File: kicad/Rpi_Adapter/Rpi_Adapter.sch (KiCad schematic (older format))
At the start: 4 parts, among them P1 CONN_02X20, P2 CONN_02X03

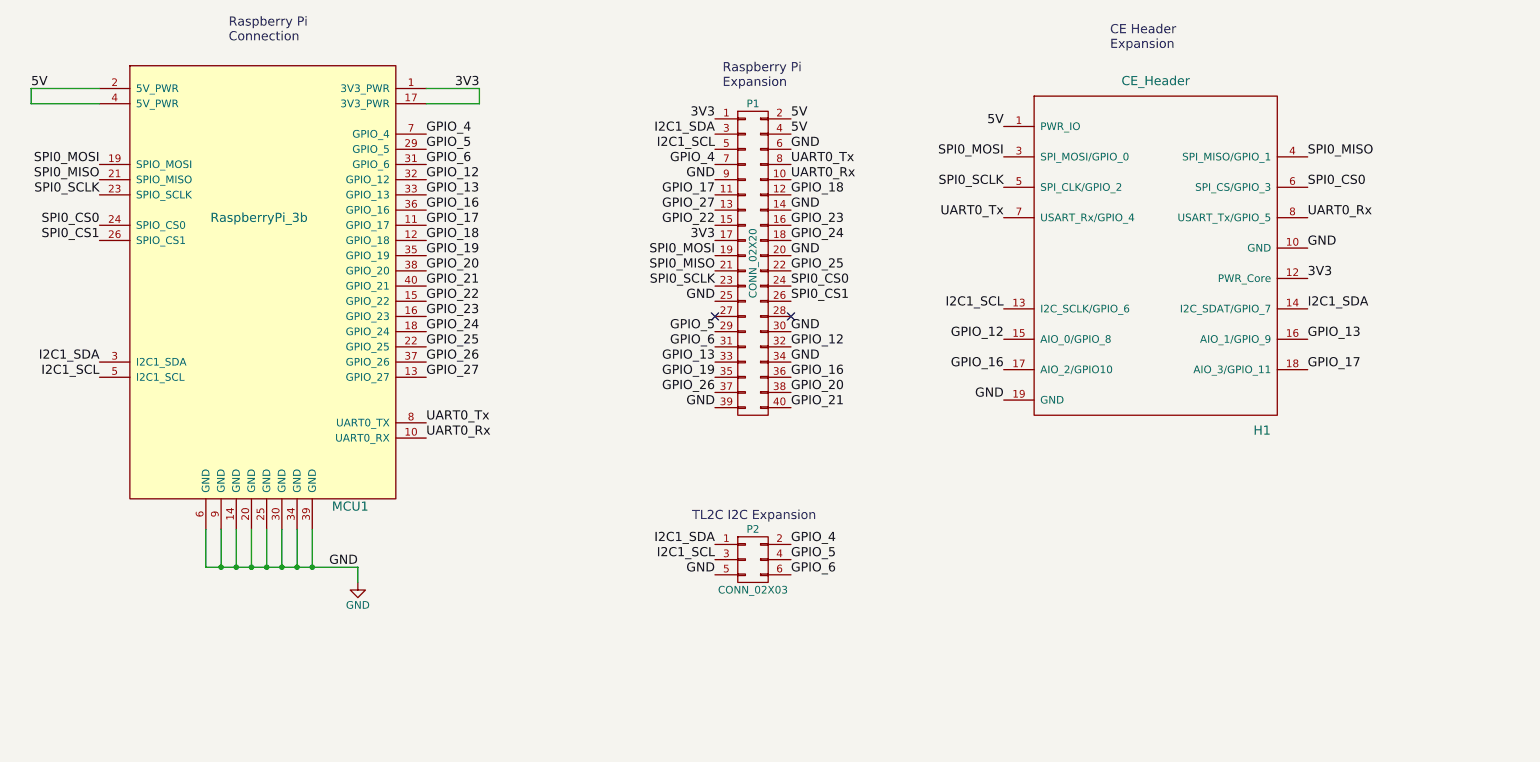
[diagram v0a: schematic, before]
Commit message: Layout done and 2L_1 is sent to OSH Park
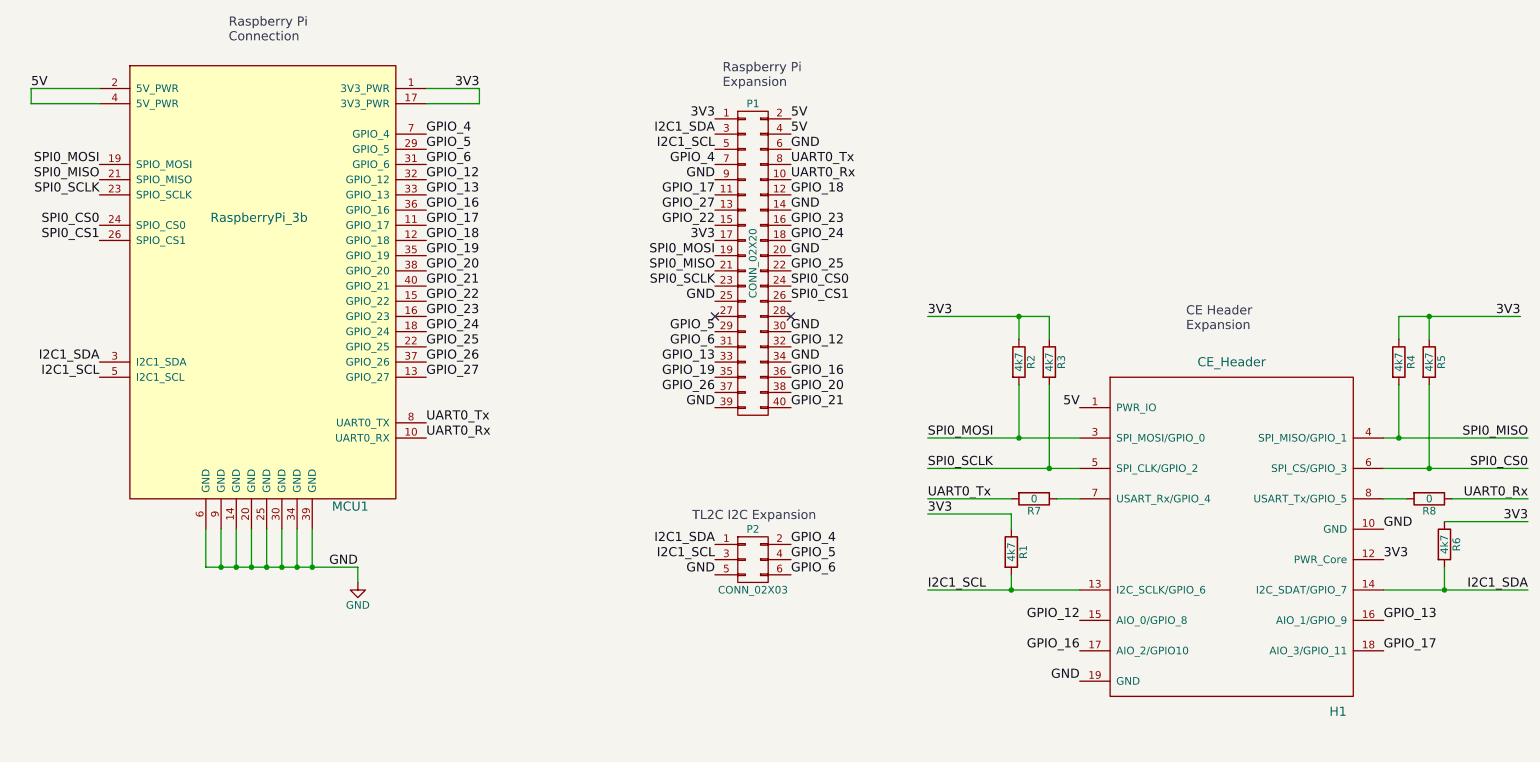
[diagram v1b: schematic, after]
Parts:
- added R1, R2, R3, R4, R5, R6: 4k7, Resistors_SMD:R_0805, symbol R
- added R7, R8: 0, Resistors_SMD:R_0805, symbol R
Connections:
- net 3V3: now also R1.1, R2.1, R3.1, R4.1, R5.1, R6.1
- net I2C1_SCL: now also R1.2
- net I2C1_SDA: now also R6.2
- net SPI0_CS0: now also R5.2
- net SPI0_MISO: now also R4.2
- net SPI0_MOSI: now also R2.2
- net SPI0_SCLK: now also R3.2
- net UART0_Rx: now also R8.1; no longer H1.8 (USART_Tx/GPIO_5)
- net UART0_Tx: now also R7.2; no longer H1.7 (USART_Rx/GPIO_4)
- new net: H1.7 (USART_Rx/GPIO_4), R7.1
- new net: H1.8 (USART_Tx/GPIO_5), R8.2
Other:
- moved on the sheet: H1
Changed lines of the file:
@@
 L CE_Header H1
 U 1 1 594798FD
-P 8500 2550
-F 0 "H1" H 9200 1350 60  0000 C CNN
-F 1 "CE_Header" H 8500 3650 60  0000 C CNN
-F 2 "CE_Header:CE_Header" H 8100 2950 60  0001 C CNN
-F 3 "" H 8100 2950 60  0000 C CNN
-	1    8500 2550
+P 9000 4400
+F 0 "H1" H 9700 3200 60  0000 C CNN
+F 1 "CE_Header" H 9000 5500 60  0000 C CNN
+F 2 "CE_Header:CE_Header" H 8600 4800 60  0001 C CNN
+F 3 "" H 8600 4800 60  0000 C CNN
+	1    9000 4400
 	1    0    0    -1
 $EndComp
@@
 Text Label 1550 3400 2    60   ~ 0
 I2C1_SCL
-Wire Wire Line
-	2250 4400 2250 4650
-Wire Wire Line
-	2250 4650 3250 4650
-Wire Wire Line
-	2950 4650 2950 4400
-Wire Wire Line
-	2350 4400 2350 4650
-Connection ~ 2350 4650
-Wire Wire Line
-	2450 4400 2450 4650
-Connection ~ 2450 4650
-Wire Wire Line
-	2550 4400 2550 4650
-Connection ~ 2550 4650
-Wire Wire Line
-	2650 4400 2650 4650
-Connection ~ 2650 4650
-Wire Wire Line
-	2750 4400 2750 4650
-Connection ~ 2750 4650
-Wire Wire Line
-	2850 4400 2850 4650
-Connection ~ 2850 4650
-$Comp
-L GND #PWR01
+$Comp
+L GND #PWR1
 U 1 1 5947A28B
 P 3250 4750
-F 0 "#PWR01" H 3250 4500 50  0001 C CNN
+F 0 "#PWR1" H 3250 4500 50  0001 C CNN
 F 1 "GND" H 3250 4600 50  0000 C CNN
 F 2 "" H 3250 4750 60  0000 C CNN
@@
 	1    0    0    -1
 $EndComp
-Wire Wire Line
-	3250 4650 3250 4750
-Connection ~ 2950 4650
 Text Label 3250 4650 2    60   ~ 0
 GND
@@
 Text Label 3700 2800 0    60   ~ 0
 GPIO_21
-Wire Wire Line
-	1550 1600 1100 1600
-Wire Wire Line
-	1100 1600 1100 1500
-Wire Wire Line
-	1100 1500 1550 1500
-Wire Wire Line
-	3700 1600 4050 1600
-Wire Wire Line
-	4050 1600 4050 1500
-Wire Wire Line
-	4050 1500 3700 1500
-Text Label 7500 1750 2    60   ~ 0
+Text Label 8000 3600 2    60   ~ 0
 5V
-Text Label 9500 2750 0    60   ~ 0
-3V3
-Text Label 7500 1950 2    60   ~ 0
+Text Label 10000 4600 0    60   ~ 0
+3V3
+Text Label 7000 3800 0    60   ~ 0
 SPI0_MOSI
-Text Label 9500 1950 0    60   ~ 0
+Text Label 10950 3800 2    60   ~ 0
 SPI0_MISO
-Text Label 7500 2150 2    60   ~ 0
+Text Label 7000 4000 0    60   ~ 0
 SPI0_SCLK
-Text Label 7500 2350 2    60   ~ 0
+Text Label 7000 4200 0    60   ~ 0
 UART0_Tx
-Text Label 9500 2350 0    60   ~ 0
+Text Label 10950 4200 2    60   ~ 0
 UART0_Rx
-Text Label 7500 3550 2    60   ~ 0
-GND
-Text Label 9500 2550 0    60   ~ 0
-GND
-Text Label 9500 2950 0    60   ~ 0
+Text Label 8000 5400 2    60   ~ 0
+GND
+Text Label 10000 4400 0    60   ~ 0
+GND
+Text Label 10950 4800 2    60   ~ 0
 I2C1_SDA
-Text Label 7500 2950 2    60   ~ 0
+Text Label 7000 4800 0    60   ~ 0
 I2C1_SCL
-Text Label 9500 2150 0    60   ~ 0
+Text Label 10950 4000 2    60   ~ 0
 SPI0_CS0
 Text Label 5600 4500 2    60   ~ 0
@@
 Text Label 6100 4700 0    60   ~ 0
 GPIO_6
-Text Label 7500 3150 2    60   ~ 0
+Text Label 8000 5000 2    60   ~ 0
 GPIO_12
-Text Label 9500 3150 0    60   ~ 0
+Text Label 10000 5000 0    60   ~ 0
 GPIO_13
-Text Label 7500 3350 2    60   ~ 0
+Text Label 8000 5200 2    60   ~ 0
 GPIO_16
-Text Label 9500 3350 0    60   ~ 0
+Text Label 10000 5200 0    60   ~ 0
 GPIO_17
 Text Notes 5650 1500 0    60   ~ 0
@@
 Text Notes 5450 4350 0    60   ~ 0
 TL2C I2C Expansion
-Text Notes 8200 1250 0    60   ~ 0
+Text Notes 8700 3100 0    60   ~ 0
 CE Header\nExpansion
 Text Notes 2400 1200 0    60   ~ 0
 Raspberry Pi\nConnection
+Wire Wire Line
+	2250 4400 2250 4650
+Wire Wire Line
+	2250 4650 3250 4650
+Wire Wire Line
+	2950 4650 2950 4400
+Wire Wire Line
+	2350 4400 2350 4650
+Connection ~ 2350 4650
+Wire Wire Line
+	2450 4400 2450 4650
+Connection ~ 2450 4650
+Wire Wire Line
+	2550 4400 2550 4650
+Connection ~ 2550 4650
+Wire Wire Line
+	2650 4400 2650 4650
+Connection ~ 2650 4650
+Wire Wire Line
+	2750 4400 2750 4650
+Connection ~ 2750 4650
+Wire Wire Line
+	2850 4400 2850 4650
+Connection ~ 2850 4650
+Wire Wire Line
+	3250 4650 3250 4750
+Connection ~ 2950 4650
+Wire Wire Line
+	1550 1600 1100 1600
+Wire Wire Line
+	1100 1600 1100 1500
+Wire Wire Line
+	1100 1500 1550 1500
+Wire Wire Line
+	3700 1600 4050 1600
+Wire Wire Line
+	4050 1600 4050 1500
+Wire Wire Line
+	4050 1500 3700 1500
+Wire Wire Line
+	8000 3800 7000 3800
+Wire Wire Line
+	8000 4000 7000 4000
+Wire Wire Line
+	10000 3800 10950 3800
+Wire Wire Line
+	10000 4000 10950 4000
+Wire Wire Line
+	10000 4800 10950 4800
+Wire Wire Line
+	8000 4800 7000 4800
+$Comp
+L R R2
+U 1 1 594806C0
+P 7600 3300
+F 0 "R2" V 7680 3300 50  0000 C CNN
+F 1 "4k7" V 7600 3300 50  0000 C CNN
+F 2 "Resistors_SMD:R_0805" V 7530 3300 30  0001 C CNN
+F 3 "" H 7600 3300 30  0000 C CNN
+	1    7600 3300
+	1    0    0    -1
+$EndComp
+$Comp
+L R R3
+U 1 1 59480738
+P 7800 3300
+F 0 "R3" V 7880 3300 50  0000 C CNN
+F 1 "4k7" V 7800 3300 50  0000 C CNN
+F 2 "Resistors_SMD:R_0805" V 7730 3300 30  0001 C CNN
+F 3 "" H 7800 3300 30  0000 C CNN
+	1    7800 3300
+	1    0    0    -1
+$EndComp
+Wire Wire Line
+	7600 3450 7600 3800
+Connection ~ 7600 3800
+Wire Wire Line
+	7800 3450 7800 4000
+Connection ~ 7800 4000
+Wire Wire Line
+	7800 3000 7800 3150
+Wire Wire Line
+	7000 3000 7800 3000
+Wire Wire Line
+	7600 3000 7600 3150
+Connection ~ 7600 3000
+Text Label 7000 3000 0    60   ~ 0
+3V3
+$Comp
+L R R1
+U 1 1 594808E4
+P 7550 4550
+F 0 "R1" V 7630 4550 50  0000 C CNN
+F 1 "4k7" V 7550 4550 50  0000 C CNN
+F 2 "Resistors_SMD:R_0805" V 7480 4550 30  0001 C CNN
+F 3 "" H 7550 4550 30  0000 C CNN
+	1    7550 4550
+	1    0    0    -1
+$EndComp
+Wire Wire Line
+	7550 4800 7550 4700
+Connection ~ 7550 4800
+Wire Wire Line
+	7550 4400 7550 4300
+Wire Wire Line
+	7550 4300 7000 4300
+Text Label 7000 4300 0    60   ~ 0
+3V3
+$Comp
+L R R4
+U 1 1 594809B3
+P 10100 3300
+F 0 "R4" V 10180 3300 50  0000 C CNN
+F 1 "4k7" V 10100 3300 50  0000 C CNN
+F 2 "Resistors_SMD:R_0805" V 10030 3300 30  0001 C CNN
+F 3 "" H 10100 3300 30  0000 C CNN
+	1    10100 3300
+	1    0    0    -1
+$EndComp
+$Comp
+L R R5
+U 1 1 59480A2F
+P 10300 3300
+F 0 "R5" V 10380 3300 50  0000 C CNN
+F 1 "4k7" V 10300 3300 50  0000 C CNN
+F 2 "Resistors_SMD:R_0805" V 10230 3300 30  0001 C CNN
+F 3 "" H 10300 3300 30  0000 C CNN
+	1    10300 3300
+	1    0    0    -1
+$EndComp
+Wire Wire Line
+	10100 3450 10100 3800
+Connection ~ 10100 3800
+Wire Wire Line
+	10300 3450 10300 4000
+Connection ~ 10300 4000
+Wire Wire Line
+	10100 3150 10100 3000
+Wire Wire Line
+	10100 3000 10900 3000
+Wire Wire Line
+	10300 3000 10300 3150
+Connection ~ 10300 3000
+$Comp
+L R R6
+U 1 1 59480C1D
+P 10400 4500
+F 0 "R6" V 10480 4500 50  0000 C CNN
+F 1 "4k7" V 10400 4500 50  0000 C CNN
+F 2 "Resistors_SMD:R_0805" V 10330 4500 30  0001 C CNN
+F 3 "" H 10400 4500 30  0000 C CNN
+	1    10400 4500
+	1    0    0    -1
+$EndComp
+Wire Wire Line
+	10400 4800 10400 4650
+Connection ~ 10400 4800
+Wire Wire Line
+	10400 4350 10950 4350
+Text Label 10950 4350 2    60   ~ 0
+3V3
+Text Label 10900 3000 2    60   ~ 0
+3V3
+$Comp
+L R R8
+U 1 1 59483847
+P 10300 4200
+F 0 "R8" V 10380 4200 50  0000 C CNN
+F 1 "0" V 10300 4200 50  0000 C CNN
+F 2 "Resistors_SMD:R_0805" V 10230 4200 30  0001 C CNN
+F 3 "" H 10300 4200 30  0000 C CNN
+	1    10300 4200
+	0    1    1    0
+$EndComp
+Wire Wire Line
+	10000 4200 10150 4200
+Wire Wire Line
+	10450 4200 10950 4200
+$Comp
+L R R7
+U 1 1 59483A0A
+P 7700 4200
+F 0 "R7" V 7780 4200 50  0000 C CNN
+F 1 "0" V 7700 4200 50  0000 C CNN
+F 2 "Resistors_SMD:R_0805" V 7630 4200 30  0001 C CNN
+F 3 "" H 7700 4200 30  0000 C CNN
+	1    7700 4200
+	0    1    1    0
+$EndComp
+Wire Wire Line
+	8000 4200 7850 4200
+Wire Wire Line
+	7550 4200 7000 4200
 $EndSCHEMATC
